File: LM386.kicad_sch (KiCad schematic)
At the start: 14 parts, among them J1 Conn_01x02_Pin, J2 Conn_01x02_Pin, U1 LM386, U2 LM386

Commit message: Add comments and fix errors
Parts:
- removed R13, R15: 1k, FM Radio:3362P_1, symbol Device:R_Trim
- added VR1, VR2: 3362P-1-102LF, 3362P_1, symbol 3362P-1-102LF:3362P-1-102LF
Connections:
- net GND: now also VR1.3 (CW), VR2.3 (CW)
- net at C14.1: now also VR1.2 (WIPER)
- net at U1.1 (GAIN): now also VR1.1 (CCW)
- net at C15.1: now also VR2.2 (WIPER)
- net at U2.1 (GAIN): now also VR2.1 (CCW)

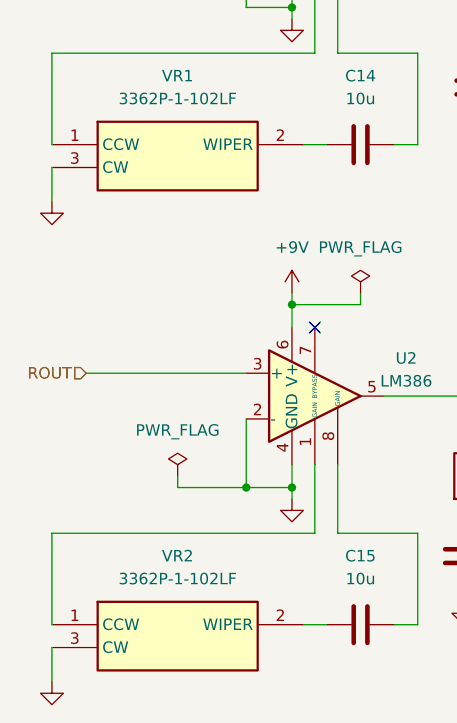
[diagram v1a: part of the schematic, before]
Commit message: Fix grounding mistake with the trimmers
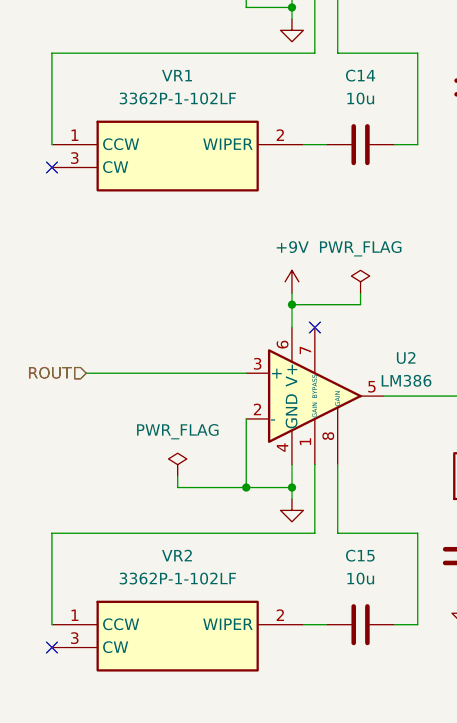
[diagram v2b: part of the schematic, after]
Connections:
- net GND: no longer VR1.3 (CW), VR2.3 (CW)
- no-connect marks 2 -> 4
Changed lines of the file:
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@@
   (junction (at 130.81 69.85) (diameter 0) (color 0 0 0 0)
   )
+  (no_connect (at 104.14 140.97))
+  (no_connect (at 104.14 87.63))
   (no_connect (at 133.35 105.41))
   (no_connect (at 133.35 52.07))
@@
     (stroke (width 0) (type default))
   )
-  (wire (pts (xy 104.14 87.63) (xy 104.14 91.44))
-    (stroke (width 0) (type default))
-  )
   (wire (pts (xy 151.13 73.66) (xy 151.13 74.93))
     (stroke (width 0) (type default))
@@
   )
   (wire (pts (xy 130.81 67.31) (xy 130.81 69.85))
-    (stroke (width 0) (type default))
-  )
-  (wire (pts (xy 104.14 140.97) (xy 104.14 144.78))
     (stroke (width 0) (type default))
   )
@@
     )
   )
-  (symbol (lib_id "power:GND") (at 104.14 144.78 0) (unit 1)
-    (in_bom yes) (on_board yes) (dnp no) (fields_autoplaced)
-    (property "Reference" "#PWR02" (at 104.14 151.13 0)
-      (effects (font (size 1.27 1.27)) hide)
-    )
-    (property "Value" "GND" (at 104.14 149.86 0)
-      (effects (font (size 1.27 1.27)) hide)
-    )
-    (property "Footprint" "" (at 104.14 144.78 0)
-      (effects (font (size 1.27 1.27)) hide)
-    )
-    (property "Datasheet" "" (at 104.14 144.78 0)
-      (effects (font (size 1.27 1.27)) hide)
-    )
-    (pin "1")
-    (instances
-      (project "FM Radio"
-        (path "/d6e904b8-5922-4df1-ad6d-648c94b6d880"
-          (reference "#PWR02") (unit 1)
-        )
-        (path "/d6e904b8-5922-4df1-ad6d-648c94b6d880/7d060ee5-a7b5-4e8e-ad6b-b389d7669048"
-          (reference "#PWR031") (unit 1)
-        )
-      )
-    )
-  )
   (symbol (lib_id "power:PWR_FLAG") (at 138.43 101.6 0) (unit 1)
     (in_bom yes) (on_board yes) (dnp no) (fields_autoplaced)
@@
         )
       )
-    )
-  )
-  (symbol (lib_id "power:GND") (at 104.14 91.44 0) (unit 1)
-    (in_bom yes) (on_board yes) (dnp no) (fields_autoplaced)
-    (property "Reference" "#PWR02" (at 104.14 97.79 0)
-      (effects (font (size 1.27 1.27)) hide)
-    )
-    (property "Value" "GND" (at 104.14 96.52 0)
-      (effects (font (size 1.27 1.27)) hide)
-    )
-    (property "Footprint" "" (at 104.14 91.44 0)
-      (effects (font (size 1.27 1.27)) hide)
-    )
-    (property "Datasheet" "" (at 104.14 91.44 0)
-      (effects (font (size 1.27 1.27)) hide)
-    )
-    (pin "1")
-    (instances
-      (project "FM Radio"
-        (path "/d6e904b8-5922-4df1-ad6d-648c94b6d880"
-          (reference "#PWR02") (unit 1)
-        )
-        (path "/d6e904b8-5922-4df1-ad6d-648c94b6d880/7d060ee5-a7b5-4e8e-ad6b-b389d7669048"
-          (reference "#PWR032") (unit 1)
-        )
-      )

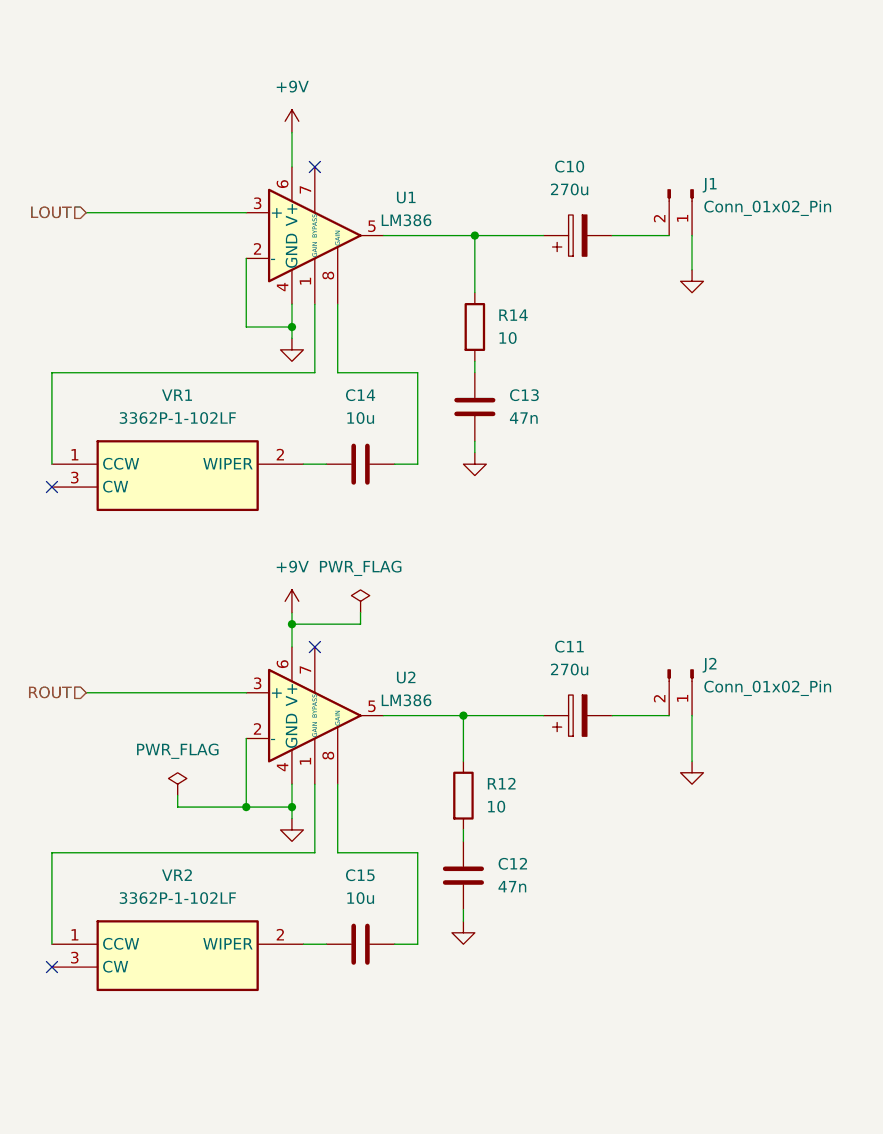
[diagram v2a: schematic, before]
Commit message: Add bypass caps to LM386
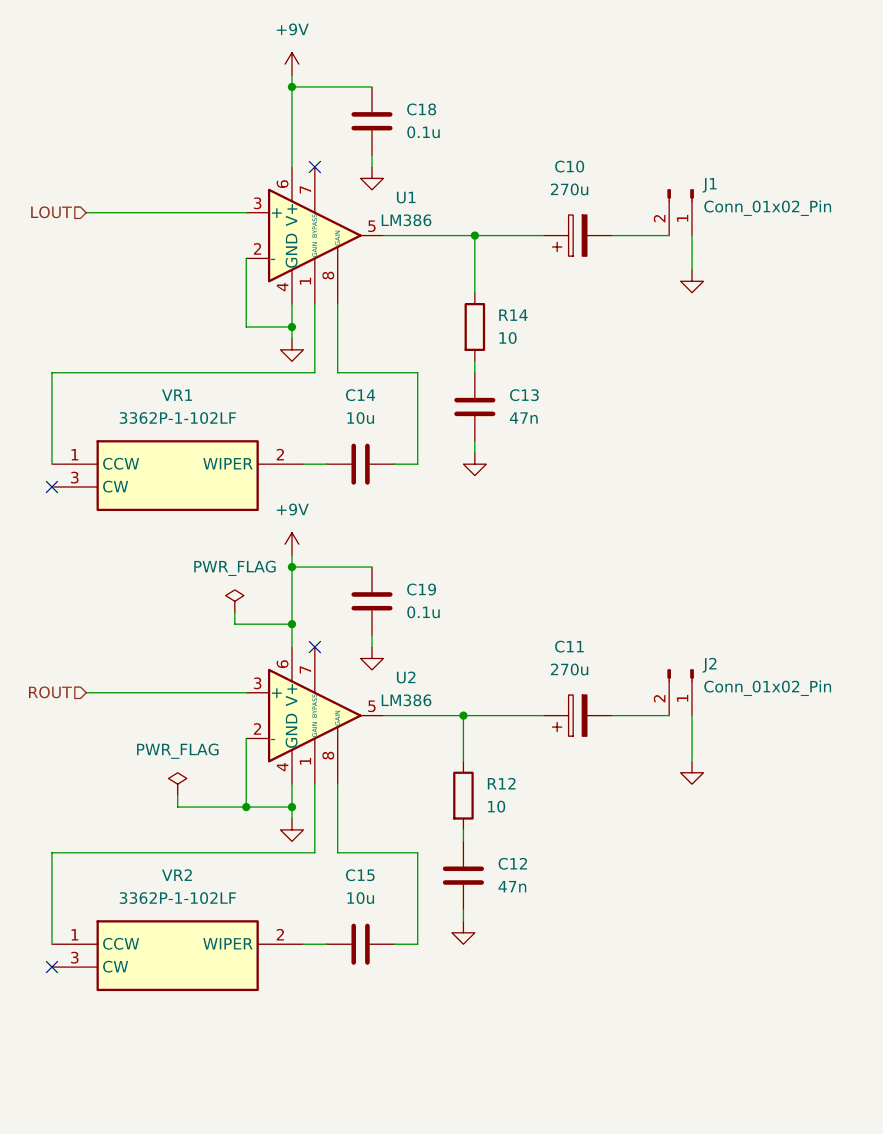
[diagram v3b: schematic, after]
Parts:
- added C18, C19: 0.1u, Capacitor_SMD:C_0603_1608Metric, symbol Device:C
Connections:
- net +9V: now also C18.2, C19.2
- net GND: now also C18.1, C19.1
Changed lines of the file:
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@@
   (junction (at 130.81 69.85) (diameter 0) (color 0 0 0 0)
+  )
+  (junction (at 130.81 96.52) (diameter 0) (color 0 0 0 0)
+  )
+  (junction (at 130.81 43.18) (diameter 0) (color 0 0 0 0)
   )
   (no_connect (at 104.14 140.97))
@@
   (no_connect (at 133.35 105.41))
   (no_connect (at 133.35 52.07))
+  (wire (pts (xy 130.81 43.18) (xy 130.81 52.07))
+    (stroke (width 0) (type default))
+  )
   (wire (pts (xy 118.11 123.19) (xy 118.11 121.92))
     (stroke (width 0) (type default))
@@
     (stroke (width 0) (type default))
   )
-  (wire (pts (xy 138.43 102.87) (xy 138.43 101.6))
+  (wire (pts (xy 139.7 50.8) (xy 139.7 52.07))
+    (stroke (width 0) (type default))
+  )
+  (wire (pts (xy 124.46 102.87) (xy 124.46 101.6))
+    (stroke (width 0) (type default))
+  )
+  (wire (pts (xy 130.81 96.52) (xy 130.81 95.25))
     (stroke (width 0) (type default))
   )
@@
     (stroke (width 0) (type default))
   )
+  (wire (pts (xy 130.81 96.52) (xy 130.81 102.87))
+    (stroke (width 0) (type default))
+  )
   (wire (pts (xy 107.95 57.15) (xy 125.73 57.15))
     (stroke (width 0) (type default))
@@
     (stroke (width 0) (type default))
   )
-  (wire (pts (xy 130.81 102.87) (xy 130.81 101.6))
-    (stroke (width 0) (type default))
-  )
   (wire (pts (xy 104.14 128.27) (xy 133.35 128.27))
     (stroke (width 0) (type default))
@@
     (stroke (width 0) (type default))
   )
+  (wire (pts (xy 130.81 96.52) (xy 139.7 96.52))
+    (stroke (width 0) (type default))
+  )
+  (wire (pts (xy 130.81 43.18) (xy 139.7 43.18))
+    (stroke (width 0) (type default))
+  )
   (wire (pts (xy 166.37 59.69) (xy 172.72 59.69))
     (stroke (width 0) (type default))
@@
     (stroke (width 0) (type default))
   )
+  (wire (pts (xy 139.7 104.14) (xy 139.7 105.41))
+    (stroke (width 0) (type default))
+  )
   (wire (pts (xy 125.73 69.85) (xy 130.81 69.85))
     (stroke (width 0) (type default))
@@
     (stroke (width 0) (type default))
   )
-  (wire (pts (xy 130.81 48.26) (xy 130.81 52.07))
-    (stroke (width 0) (type default))
-  )
-  (wire (pts (xy 130.81 102.87) (xy 138.43 102.87))
+  (wire (pts (xy 130.81 41.91) (xy 130.81 43.18))
+    (stroke (width 0) (type default))
+  )
+  (wire (pts (xy 124.46 102.87) (xy 130.81 102.87))
     (stroke (width 0) (type default))
   )
@@
     )
   )
+  (symbol (lib_id "power:GND") (at 139.7 52.07 0) (unit 1)
+    (in_bom yes) (on_board yes) (dnp no) (fields_autoplaced)
+    (property "Reference" "#PWR02" (at 139.7 58.42 0)
+      (effects (font (size 1.27 1.27)) hide)
+    )
+    (property "Value" "GND" (at 139.7 57.15 0)
+      (effects (font (size 1.27 1.27)) hide)
+    )
+    (property "Footprint" "" (at 139.7 52.07 0)
+      (effects (font (size 1.27 1.27)) hide)
+    )
+    (property "Datasheet" "" (at 139.7 52.07 0)
+      (effects (font (size 1.27 1.27)) hide)
+    )
+    (pin "1")
+    (instances
+      (project "FM Radio"
+        (path "/d6e904b8-5922-4df1-ad6d-648c94b6d880"
+          (reference "#PWR02") (unit 1)
+        )
+        (path "/d6e904b8-5922-4df1-ad6d-648c94b6d880/7d060ee5-a7b5-4e8e-ad6b-b389d7669048"
+          (reference "#PWR031") (unit 1)
+        )
+      )
+    )
+  )
   (symbol (lib_id "Device:C") (at 151.13 78.74 0) (unit 1)
     (in_bom yes) (on_board yes) (dnp no) (fields_autoplaced)
@@
     )
   )
-  (symbol (lib_id "power:PWR_FLAG") (at 138.43 101.6 0) (unit 1)
-    (in_bom yes) (on_board yes) (dnp no) (fields_autoplaced)
-    (property "Reference" "#FLG02" (at 138.43 99.695 0)
-      (effects (font (size 1.27 1.27)) hide)
-    )
-    (property "Value" "PWR_FLAG" (at 138.43 96.52 0)
-      (effects (font (size 1.27 1.27)))
-    )
-    (property "Footprint" "" (at 138.43 101.6 0)
-      (effects (font (size 1.27 1.27)) hide)
-    )
-    (property "Datasheet" "~" (at 138.43 101.6 0)
+  (symbol (lib_id "power:PWR_FLAG") (at 124.46 101.6 0) (unit 1)
+    (in_bom yes) (on_board yes) (dnp no) (fields_autoplaced)
+    (property "Reference" "#FLG02" (at 124.46 99.695 0)
+      (effects (font (size 1.27 1.27)) hide)
+    )
+    (property "Value" "PWR_FLAG" (at 124.46 96.52 0)
+      (effects (font (size 1.27 1.27)))
+    )
+    (property "Footprint" "" (at 124.46 101.6 0)
+      (effects (font (size 1.27 1.27)) hide)
+    )
+    (property "Datasheet" "~" (at 124.46 101.6 0)
       (effects (font (size 1.27 1.27)) hide)
     )
@@
     )
   )
+  (symbol (lib_id "Device:C") (at 139.7 46.99 180) (unit 1)
+    (in_bom yes) (on_board yes) (dnp no) (fields_autoplaced)
+    (property "Reference" "C18" (at 143.51 45.72 0)
+      (effects (font (size 1.27 1.27)) (justify right))
+    )
+    (property "Value" "0.1u" (at 143.51 48.26 0)
+      (effects (font (size 1.27 1.27)) (justify right))
+    )
+    (property "Footprint" "Capacitor_SMD:C_0603_1608Metric" (at 138.7348 43.18 0)
+      (effects (font (size 1.27 1.27)) hide)
+    )
+    (property "Datasheet" "~" (at 139.7 46.99 0)
+      (effects (font (size 1.27 1.27)) hide)
+    )
+    (pin "1")
+    (pin "2")
+    (instances
+      (project "FM Radio"
+        (path "/d6e904b8-5922-4df1-ad6d-648c94b6d880/7d060ee5-a7b5-4e8e-ad6b-b389d7669048"
+          (reference "C18") (unit 1)
+        )
+      )
+    )
+  )
   (symbol (lib_id "power:GND") (at 151.13 83.82 0) (unit 1)
     (in_bom yes) (on_board yes) (dnp no) (fields_autoplaced)
@@
     )
   )
-  (symbol (lib_id "power:+9V") (at 130.81 101.6 0) (unit 1)
-    (in_bom yes) (on_board yes) (dnp no) (fields_autoplaced)
-    (property "Reference" "#PWR018" (at 130.81 105.41 0)
-      (effects (font (size 1.27 1.27)) hide)
-    )
-    (property "Value" "+9V" (at 130.81 96.52 0)
-      (effects (font (size 1.27 1.27)))
-    )
-    (property "Footprint" "" (at 130.81 101.6 0)
-      (effects (font (size 1.27 1.27)) hide)
-    )
-    (property "Datasheet" "" (at 130.81 101.6 0)
+  (symbol (lib_id "power:+9V") (at 130.81 95.25 0) (unit 1)
+    (in_bom yes) (on_board yes) (dnp no) (fields_autoplaced)
+    (property "Reference" "#PWR018" (at 130.81 99.06 0)
+      (effects (font (size 1.27 1.27)) hide)
+    )
+    (property "Value" "+9V" (at 130.81 90.17 0)
+      (effects (font (size 1.27 1.27)))
+    )
+    (property "Footprint" "" (at 130.81 95.25 0)
+      (effects (font (size 1.27 1.27)) hide)
+    )
+    (property "Datasheet" "" (at 130.81 95.25 0)
       (effects (font (size 1.27 1.27)) hide)
     )
@@
     )
   )
-  (symbol (lib_id "power:+9V") (at 130.81 48.26 0) (unit 1)
-    (in_bom yes) (on_board yes) (dnp no) (fields_autoplaced)
-    (property "Reference" "#PWR015" (at 130.81 52.07 0)
-      (effects (font (size 1.27 1.27)) hide)
-    )
-    (property "Value" "+9V" (at 130.81 43.18 0)
-      (effects (font (size 1.27 1.27)))
-    )
-    (property "Footprint" "" (at 130.81 48.26 0)
-      (effects (font (size 1.27 1.27)) hide)
-    )
-    (property "Datasheet" "" (at 130.81 48.26 0)
+  (symbol (lib_id "power:+9V") (at 130.81 41.91 0) (unit 1)
+    (in_bom yes) (on_board yes) (dnp no) (fields_autoplaced)
+    (property "Reference" "#PWR015" (at 130.81 45.72 0)
+      (effects (font (size 1.27 1.27)) hide)
+    )
+    (property "Value" "+9V" (at 130.81 36.83 0)
+      (effects (font (size 1.27 1.27)))
+    )
+    (property "Footprint" "" (at 130.81 41.91 0)
+      (effects (font (size 1.27 1.27)) hide)
+    )
+    (property "Datasheet" "" (at 130.81 41.91 0)
       (effects (font (size 1.27 1.27)) hide)
     )
@@
         )
       )
+    )
+  )
+  (symbol (lib_id "power:GND") (at 139.7 105.41 0) (unit 1)
+    (in_bom yes) (on_board yes) (dnp no) (fields_autoplaced)
+    (property "Reference" "#PWR02" (at 139.7 111.76 0)
+      (effects (font (size 1.27 1.27)) hide)
+    )
+    (property "Value" "GND" (at 139.7 110.49 0)
+      (effects (font (size 1.27 1.27)) hide)
+    )
+    (property "Footprint" "" (at 139.7 105.41 0)
+      (effects (font (size 1.27 1.27)) hide)
+    )
+    (property "Datasheet" "" (at 139.7 105.41 0)
+      (effects (font (size 1.27 1.27)) hide)
+    )
+    (pin "1")
+    (instances
+      (project "FM Radio"
+        (path "/d6e904b8-5922-4df1-ad6d-648c94b6d880"
+          (reference "#PWR02") (unit 1)
+        )
+        (path "/d6e904b8-5922-4df1-ad6d-648c94b6d880/7d060ee5-a7b5-4e8e-ad6b-b389d7669048"
+          (reference "#PWR032") (unit 1)
+        )
+      )
+    )
+  )
+  (symbol (lib_id "Device:C") (at 139.7 100.33 180) (unit 1)
+    (in_bom yes) (on_board yes) (dnp no) (fields_autoplaced)
+    (property "Reference" "C19" (at 143.51 99.06 0)
+      (effects (font (size 1.27 1.27)) (justify right))
+    )
+    (property "Value" "0.1u" (at 143.51 101.6 0)
+      (effects (font (size 1.27 1.27)) (justify right))
+    )
+    (property "Footprint" "Capacitor_SMD:C_0603_1608Metric" (at 138.7348 96.52 0)
+      (effects (font (size 1.27 1.27)) hide)
+    )
+    (property "Datasheet" "~" (at 139.7 100.33 0)
+      (effects (font (size 1.27 1.27)) hide)
+    )
+    (pin "1")
+    (pin "2")
+    (instances
+      (project "FM Radio"
+        (path "/d6e904b8-5922-4df1-ad6d-648c94b6d880/7d060ee5-a7b5-4e8e-ad6b-b389d7669048"
+          (reference "C19") (unit 1)
+        )
+      )

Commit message: Complete layout
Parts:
- R12, R14: footprint FM Radio:RESC1608X55N -> Resistor_SMD:R_0603_1608Metric
- VR1, VR2: footprint 3362P_1 -> FM Radio:3362P_1
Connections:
- net at C14.1, VR1.2 (WIPER): now also VR1.3 (CW)
- net at C15.1, VR2.2 (WIPER): now also VR2.3 (CW)
- no-connect marks 4 -> 2
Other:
- moved on the sheet: C11, C12, C15, C19, J2, R12, U2, VR2
